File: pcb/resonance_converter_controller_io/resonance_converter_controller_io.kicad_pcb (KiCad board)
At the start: 4 copper layers, 61.4 x 79.6 mm, 53 parts, among them J1 DF12NB_5.0_-20DP-0.5V_51_, J2 Conn_01x30_MountingPin, J3 Conn_01x02, J4 Conn_01x02, J7 Conn_ARM_SWD_TagConnect_TC2030, SW1 RotaryEncoder_Switch_MP, SW2 SW_SPST, SW3 SW_SPST, SW4 SW_SPST, SW5 SW_SPST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

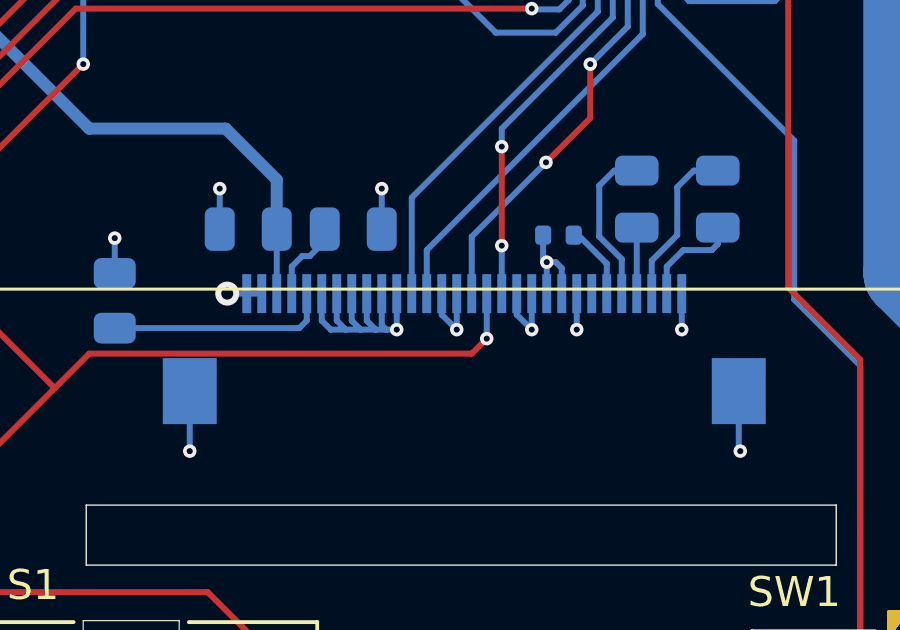
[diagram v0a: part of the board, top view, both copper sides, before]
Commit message: Kicad 9 -> 10
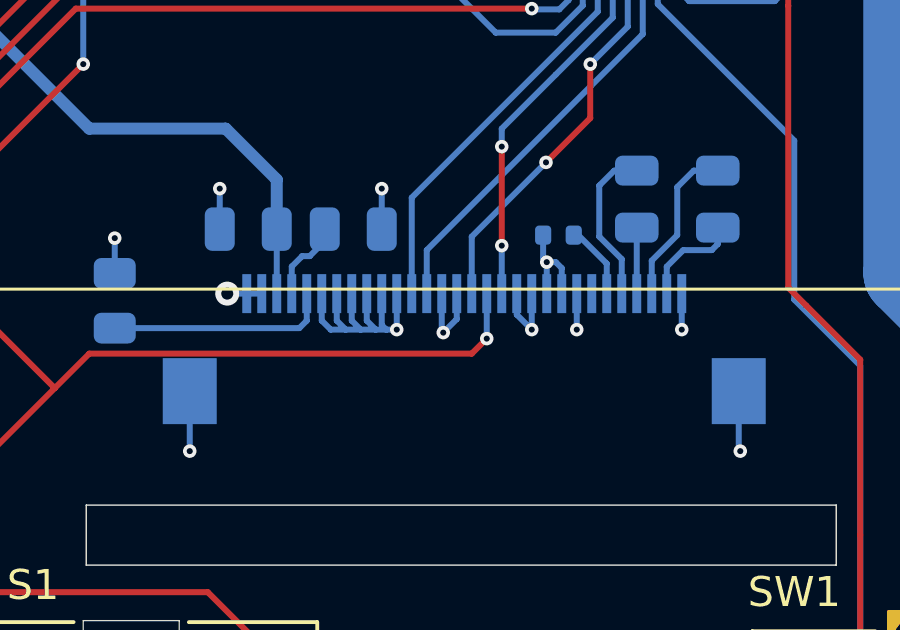
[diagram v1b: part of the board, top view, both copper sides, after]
